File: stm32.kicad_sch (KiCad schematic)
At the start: 14 parts, among them SW1 SW_Push, U1 STM32F411CEUx, Y1 Crystal_GND24

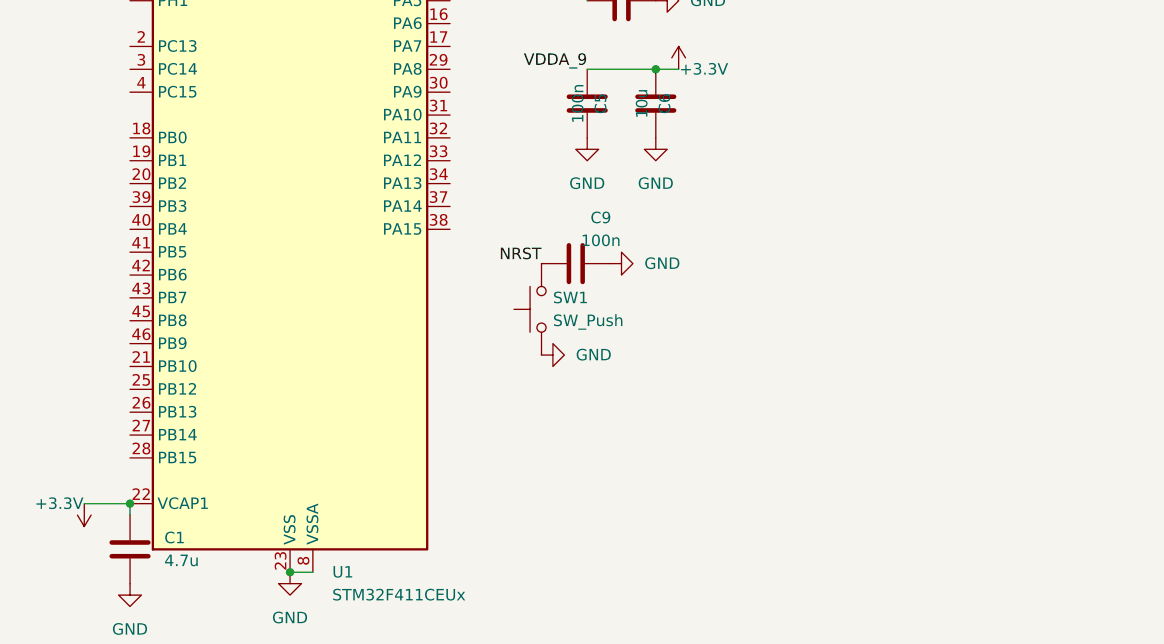
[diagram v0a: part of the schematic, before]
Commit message: SWD: complete Tag-Connect TC2030 wiring with SWO + VTref cap
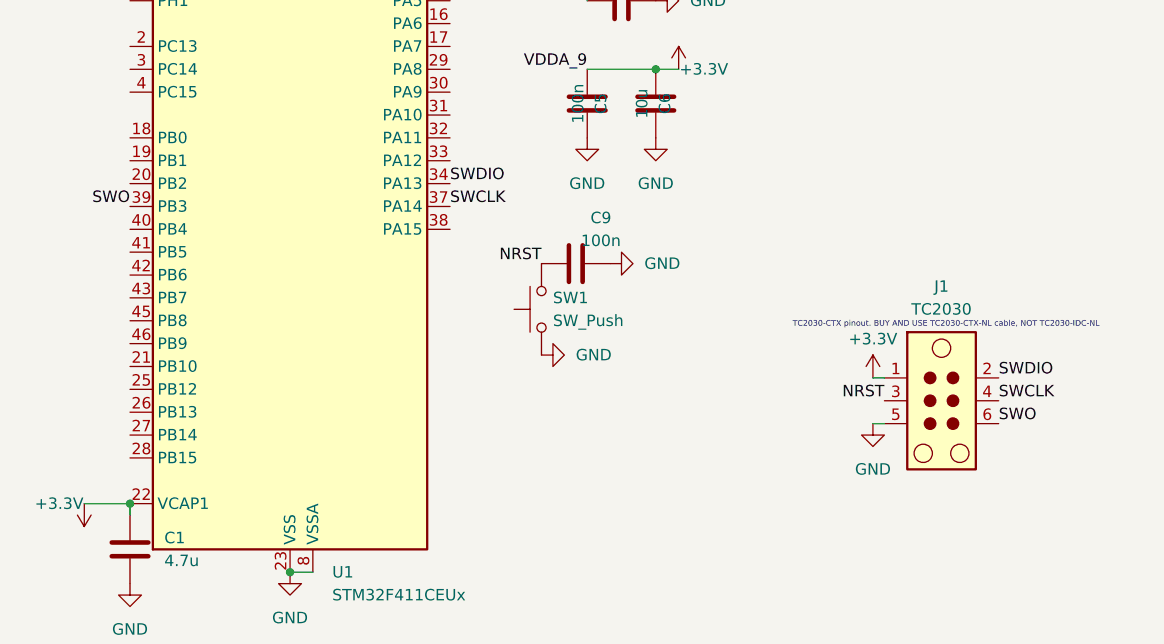
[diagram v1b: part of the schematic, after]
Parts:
- added J1: TC2030, Connector:Tag-Connect_TC2030-IDC-NL_2x03_P1.27mm_Vertical, symbol Connector:TC2030
- C2, C3, C4, C5, C7, C9: footprint (none) -> Capacitor_SMD:C_0402_1005Metric
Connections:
- net +3.3V: now also J1.1
- net GND: now also J1.5
- net NRST: now also J1.3
- net SWDIO: now reaches U1.34 (PA13)
- net SWDIO: now also J1.2
- net SWCLK: now reaches U1.37 (PA14)
- net SWCLK: now also J1.4
- net SWO: now reaches U1.39 (PB3)
- net SWO: now also J1.6
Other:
- note added: "TC2030-CTX pinout. BUY AND USE TC2030-CTX-NL cable, NOT TC2030-IDC-NL"

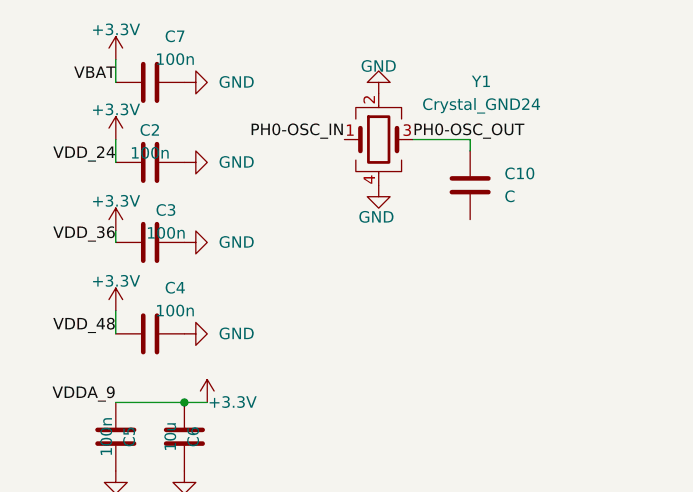
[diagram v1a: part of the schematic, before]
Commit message: fixing crystal
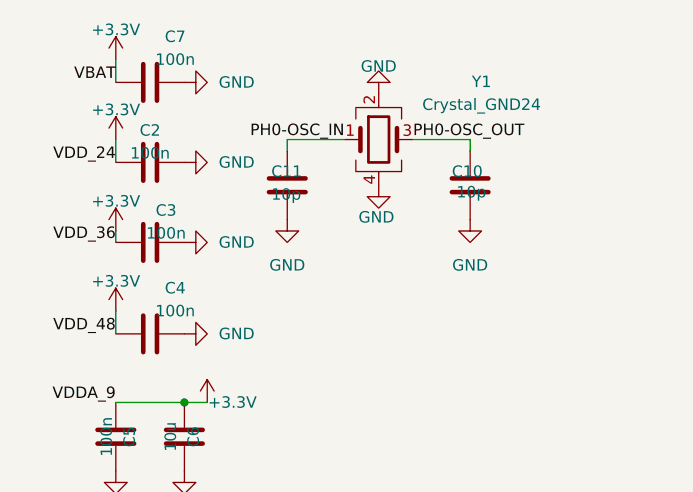
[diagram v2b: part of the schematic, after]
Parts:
- added C11: 10p, symbol Device:C
- C10: value C -> 10p
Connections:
- net GND: now also C10.1, C11.1
- net PH0-OSC_IN: now also C11.2
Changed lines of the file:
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@@
+	(wire
+		(pts
+			(xy 93.98 25.4) (xy 93.98 26.67)
+		)
+		(stroke
+			(width 0)
+			(type default)
+		)
+	)
+	(wire
+		(pts
+			(xy 100.33 25.4) (xy 93.98 25.4)
+		)
+		(stroke
+			(width 0)
+			(type default)
+		)
+	)
 	(wire
 		(pts
@@
 	(symbol
 		(lib_id "Device:C")
+		(at 93.98 30.48 180)
+		(unit 1)
+		(exclude_from_sim no)
+		(in_bom yes)
+		(on_board yes)
+		(dnp no)
+		(property "Reference" "C11"
+			(at 92.202 28.956 0)
+			(effects
+				(font
+					(size 1.27 1.27)
+				)
+				(justify right)
+			)
+		)
+		(property "Value" "10p"
+			(at 92.202 31.496 0)
+			(effects
+				(font
+					(size 1.27 1.27)
+				)
+				(justify right)
+			)
+		)
+		(property "Footprint" ""
+			(at 93.0148 26.67 0)
+			(effects
+				(font
+					(size 1.27 1.27)
+				)
+				(hide yes)
+			)
+		)
+		(property "Datasheet" "~"
+			(at 93.98 30.48 0)
+			(effects
+				(font
+					(size 1.27 1.27)
+				)
+				(hide yes)
+			)
+		)
+		(property "Description" "Unpolarized capacitor"
+			(at 93.98 30.48 0)
+			(effects
+				(font
+					(size 1.27 1.27)
+				)
+				(hide yes)
+			)
+		)
+		(pin "2"
+		)
+		(pin "1"
+		)
+		(instances
+			(project "stm32"
+				(path "/807257e6-524f-404b-b91f-049b9c2bdd5b"
+					(reference "C11")
+					(unit 1)
+				)
+			)
+		)
+	)
+	(symbol
+		(lib_id "Device:C")
 		(at 114.3 30.48 180)
 		(unit 1)
@@
 		(on_board yes)
 		(dnp no)
-		(fields_autoplaced yes)
 		(property "Reference" "C10"
-			(at 118.11 29.2099 0)
+			(at 112.268 28.956 0)
 			(effects
 				(font
@@
 			)
 		)
-		(property "Value" "C"
-			(at 118.11 31.7499 0)
+		(property "Value" "10p"
+			(at 112.776 31.242 0)
 			(effects
 				(font
@@
 	)
 	(symbol
+		(lib_id "power:GND")
+		(at 93.98 34.29 0)
+		(unit 1)
+		(exclude_from_sim no)
+		(in_bom yes)
+		(on_board yes)
+		(dnp no)
+		(fields_autoplaced yes)
+		(property "Reference" "#PWR024"
+			(at 93.98 40.64 0)
+			(effects
+				(font
+					(size 1.27 1.27)
+				)
+				(hide yes)
+			)
+		)
+		(property "Value" "GND"
+			(at 93.98 39.37 0)
+			(effects
+				(font
+					(size 1.27 1.27)
+				)
+			)
+		)
+		(property "Footprint" ""
+			(at 93.98 34.29 0)
+			(effects
+				(font
+					(size 1.27 1.27)
+				)
+				(hide yes)
+			)
+		)
+		(property "Datasheet" ""
+			(at 93.98 34.29 0)
+			(effects
+				(font
+					(size 1.27 1.27)
+				)
+				(hide yes)
+			)
+		)
+		(property "Description" "Power symbol creates a global label with name \"GND\" , ground"
+			(at 93.98 34.29 0)
+			(effects
+				(font
+					(size 1.27 1.27)
+				)
+				(hide yes)
+			)
+		)
+		(pin "1"
+		)
+		(instances
+			(project "stm32"
+				(path "/807257e6-524f-404b-b91f-049b9c2bdd5b"
+					(reference "#PWR024")
+					(unit 1)
+				)
+			)
+		)
+	)
+	(symbol
 		(lib_id "Device:C")
 		(at 73.66 76.2 90)
@@
 					(unit 1)
 				)
+			)
+		)
+	)
+	(symbol
+		(lib_id "power:GND")
+		(at 114.3 34.29 0)
+		(unit 1)
+		(exclude_from_sim no)
+		(in_bom yes)
+		(on_board yes)
+		(dnp no)
+		(fields_autoplaced yes)
+		(property "Reference" "#PWR025"
+			(at 114.3 40.64 0)
+			(effects
+				(font
+					(size 1.27 1.27)
+				)
+				(hide yes)
+			)
+		)
+		(property "Value" "GND"
+			(at 114.3 39.37 0)
+			(effects
+				(font
+					(size 1.27 1.27)
+				)
+			)
+		)
+		(property "Footprint" ""
+			(at 114.3 34.29 0)
+			(effects
+				(font
+					(size 1.27 1.27)
+				)
+				(hide yes)
+			)
+		)
+		(property "Datasheet" ""
+			(at 114.3 34.29 0)
+			(effects
+				(font
+					(size 1.27 1.27)
+				)
+				(hide yes)
+			)
+		)
+		(property "Description" "Power symbol creates a global label with name \"GND\" , ground"
+			(at 114.3 34.29 0)
+			(effects
+				(font
+					(size 1.27 1.27)
+				)
+				(hide yes)
+			)
+		)
+		(pin "1"
+		)
+		(instances
+			(project "stm32"
+				(path "/807257e6-524f-404b-b91f-049b9c2bdd5b"
+					(reference "#PWR025")
+					(unit 1)
+				)

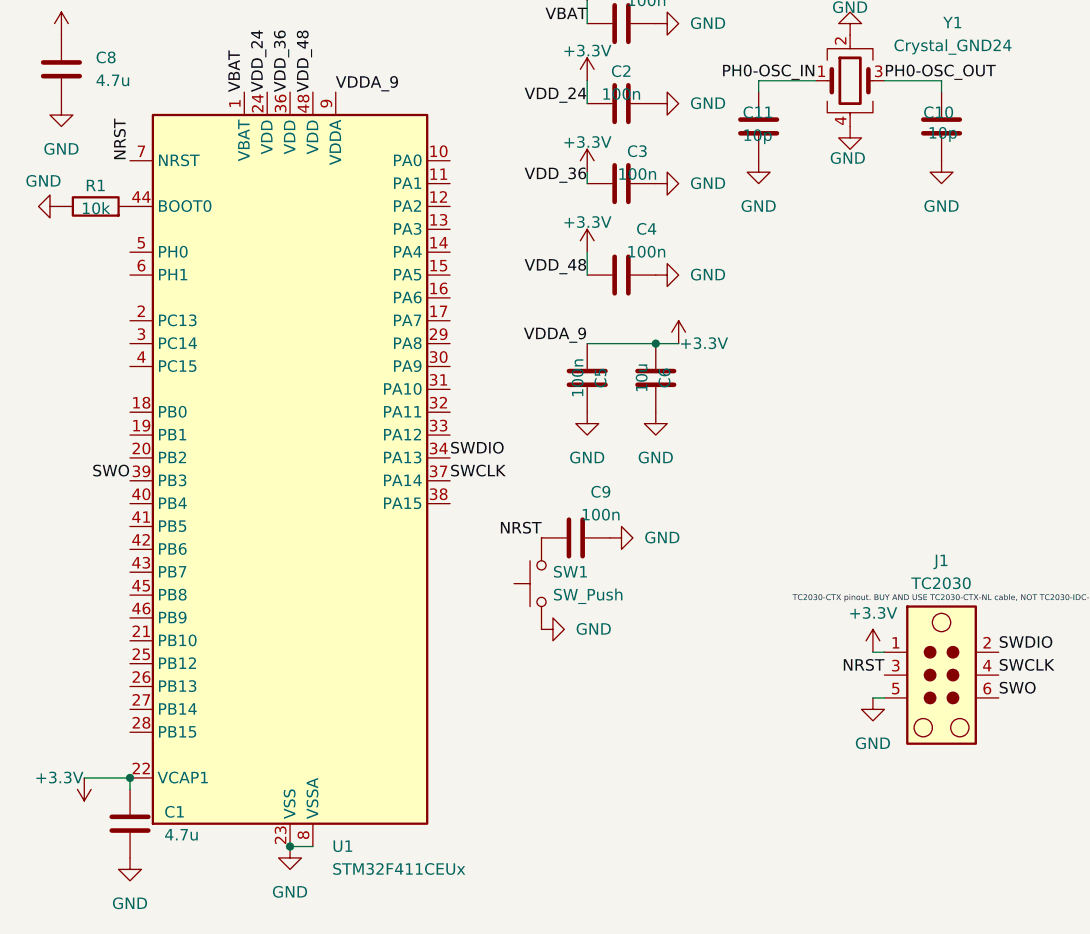
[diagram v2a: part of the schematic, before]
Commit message: SPI bus: MCU-side wiring (SPI1 = PA5/6/7, CS = PA1-4, INT = PB0/1, pull-ups on CS+MISO)
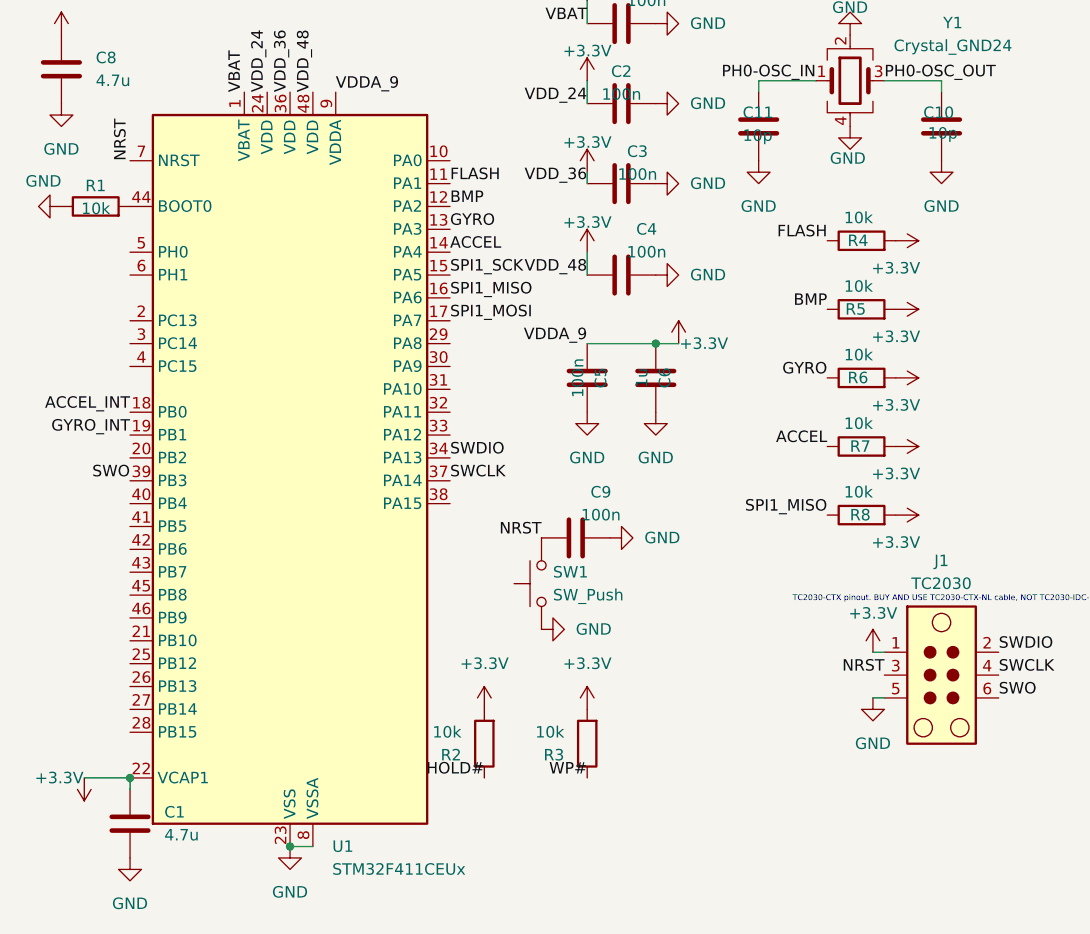
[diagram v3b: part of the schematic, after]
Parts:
- added R2, R3, R4, R5, R6, R7, R8: 10k, symbol Device:R
- C1: footprint (none) -> Capacitor_SMD:C_0603_1608Metric
- C10, C11: footprint (none) -> Capacitor_SMD:C_0402_1005Metric
- C6: value 10u -> 1u; footprint (none) -> Capacitor_SMD:C_0402_1005Metric
- SW1: footprint Button_Switch_SMD:SW_SPST_B3SN_1000P -> Button_Switch_SMD:SW_SPST_B3S-1000
- Y1: footprint (none) -> Crystal:Crystal_SMD_3225-4Pin_3.2x2.5mm
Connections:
- net +3.3V: now also R2.2, R3.2, R4.2, R5.2, R6.2, R7.2, R8.2
- net FLASH: now reaches U1.11 (PA1)
- net FLASH: now also R4.1
- net BMP: now reaches U1.12 (PA2)
- net BMP: now also R5.1
- net GYRO: now reaches U1.13 (PA3)
- net GYRO: now also R6.1
- net ACCEL: now reaches U1.14 (PA4)
- net ACCEL: now also R7.1
- net SPI1_SCK: now reaches U1.15 (PA5)
- net SPI1_MISO: now reaches U1.16 (PA6)
- net SPI1_MISO: now also R8.1
- net SPI1_MOSI: now reaches U1.17 (PA7)
- net ACCEL_INT: now reaches U1.18 (PB0)
- net GYRO_INT: now reaches U1.19 (PB1)
- new net HOLD#: R2.1
- new net WP#: R3.1

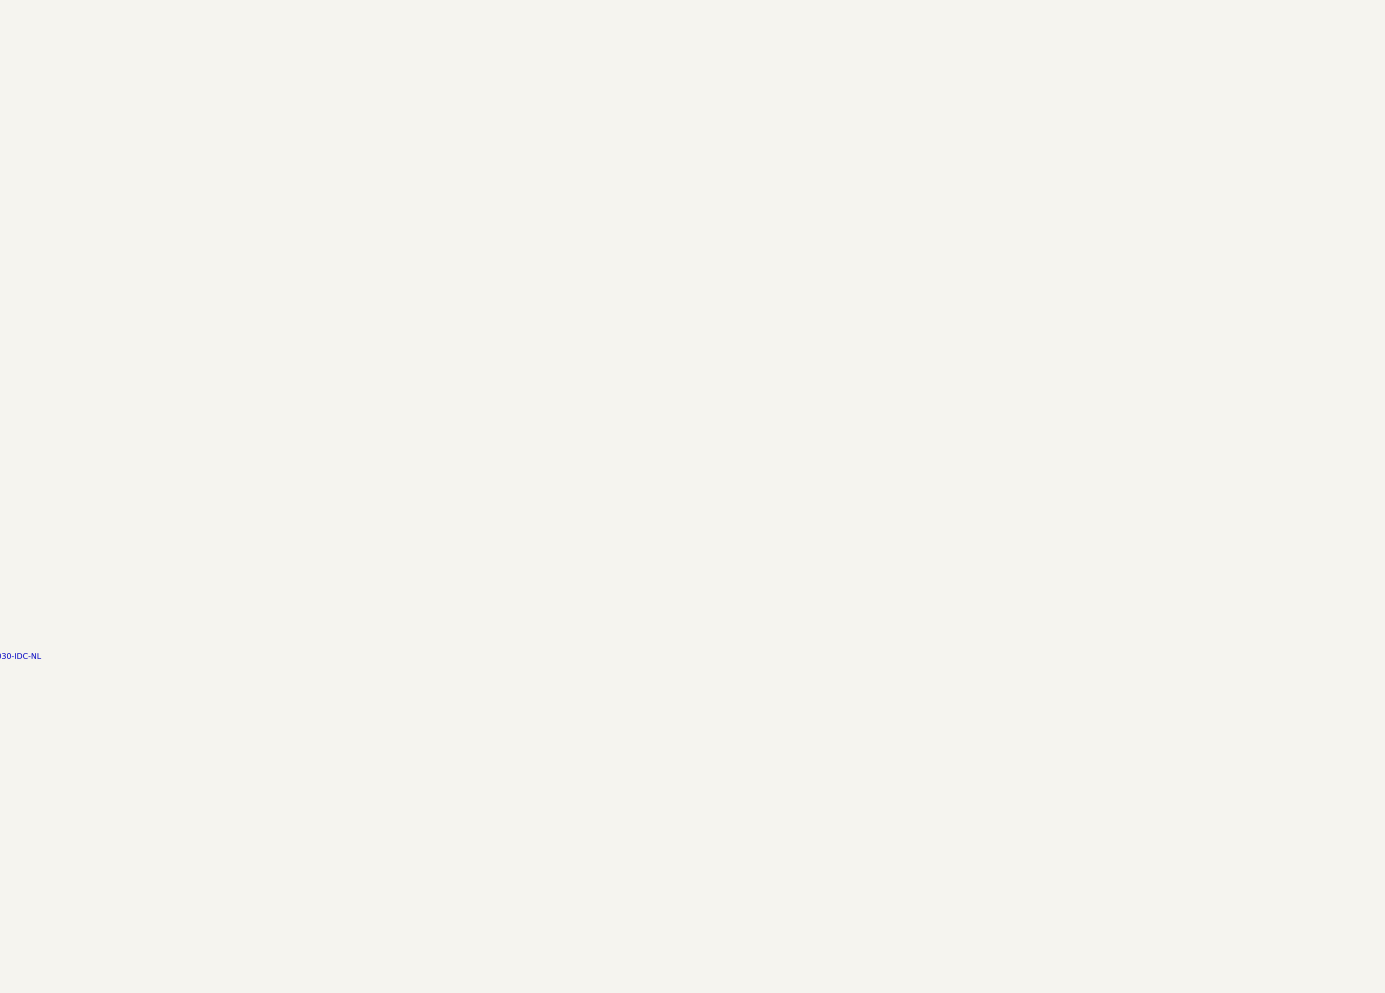
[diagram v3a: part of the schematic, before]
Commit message: SPI section: place BMI088, BMP388, W25Q128 symbols + decoupling + HOLD/WP pull-ups
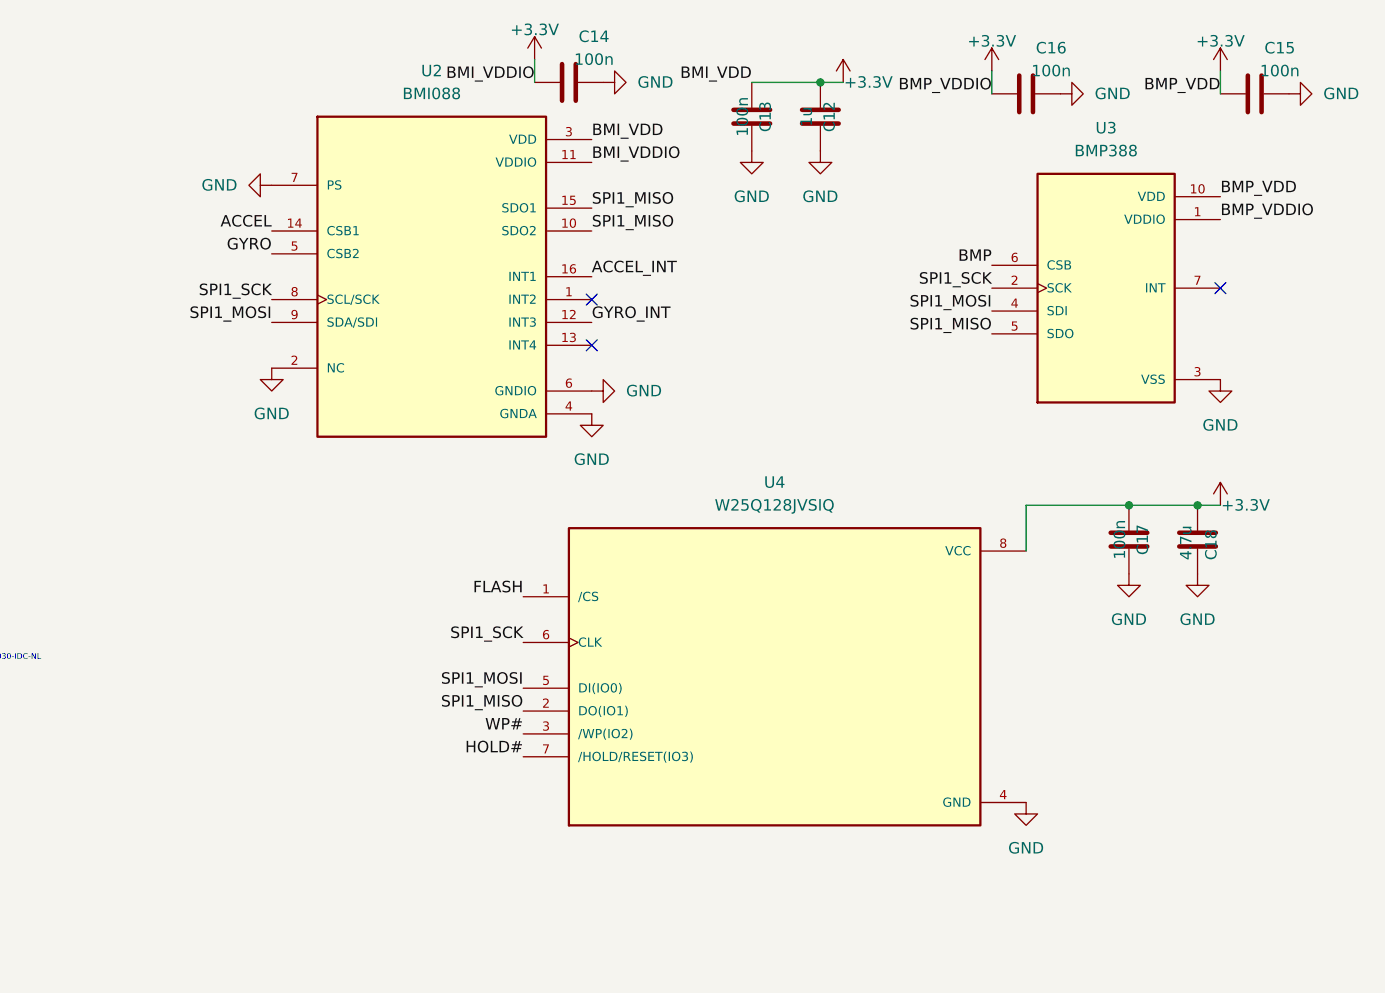
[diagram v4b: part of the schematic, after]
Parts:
- added C12: 1u, Capacitor_SMD:C_0402_1005Metric, symbol Device:C
- added C13, C14, C15, C16, C17: 100n, Capacitor_SMD:C_0402_1005Metric, symbol Device:C
- added C18: 4.7u, Capacitor_SMD:C_0603_1608Metric, symbol Device:C
- added U2: BMI088, Custom_Library:BMI088, symbol 2026-04-12_18-39-20:BMI088
- added U3: BMP388, Custom_Library:BMP388, symbol 2026-04-12_18-39-20:BMP388
- added U4: W25Q128JVSIQ, Custom_Library:W25Q128, symbol 2026-04-12_18-39-20:W25Q128JVSIQ
- R2, R3, R4, R5, R6, R7, R8: footprint (none) -> Resistor_SMD:R_0402_1005Metric
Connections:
- net +3.3V: now also C12.1, C13.1, C14.1, C15.1, C16.1, C17.1, C18.1, U2.11 (VDDIO), U2.3 (VDD), U3.1 (VDDIO), U3.10 (VDD), U4.8 (VCC)
- net ACCEL: now also U2.14 (CSB1)
- net ACCEL_INT: now also U2.16 (INT1)
- net BMP: now also U3.6 (CSB)
- net FLASH: now also U4.1 (/CS)
- net GND: now also C12.2, C13.2, C14.2, C15.2, C16.2, C17.2, C18.2, U2.2 (NC), U2.4 (GNDA), U2.6 (GNDIO), U2.7 (PS), U3.3 (VSS), U3.8 (VSS), U3.9 (VSS), U4.4 (GND)
- net GYRO: now also U2.5 (CSB2)
- net GYRO_INT: now also U2.12 (INT3)
- net HOLD#: now also U4.7 (/HOLD/RESET(IO3))
- net SPI1_MISO: now also U2.10 (SDO2), U2.15 (SDO1), U3.5 (SDO), U4.2 (DO(IO1))
- net SPI1_MOSI: now also U2.9 (SDA/SDI), U3.4 (SDI), U4.5 (DI(IO0))
- net SPI1_SCK: now also U2.8 (SCL/SCK), U3.2 (SCK), U4.6 (CLK)
- net WP#: now also U4.3 (/WP(IO2))
- no-connect marks 0 -> 3
